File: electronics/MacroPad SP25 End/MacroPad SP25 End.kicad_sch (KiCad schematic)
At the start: 14 parts, among them J1 Conn_01x07_Pin, J2 Conn_01x07_Pin, J3 Conn_01x07_Pin, J4 Conn_01x07_Pin, SW1 RotaryEncoder_Switch, SW2 RotaryEncoder_Switch

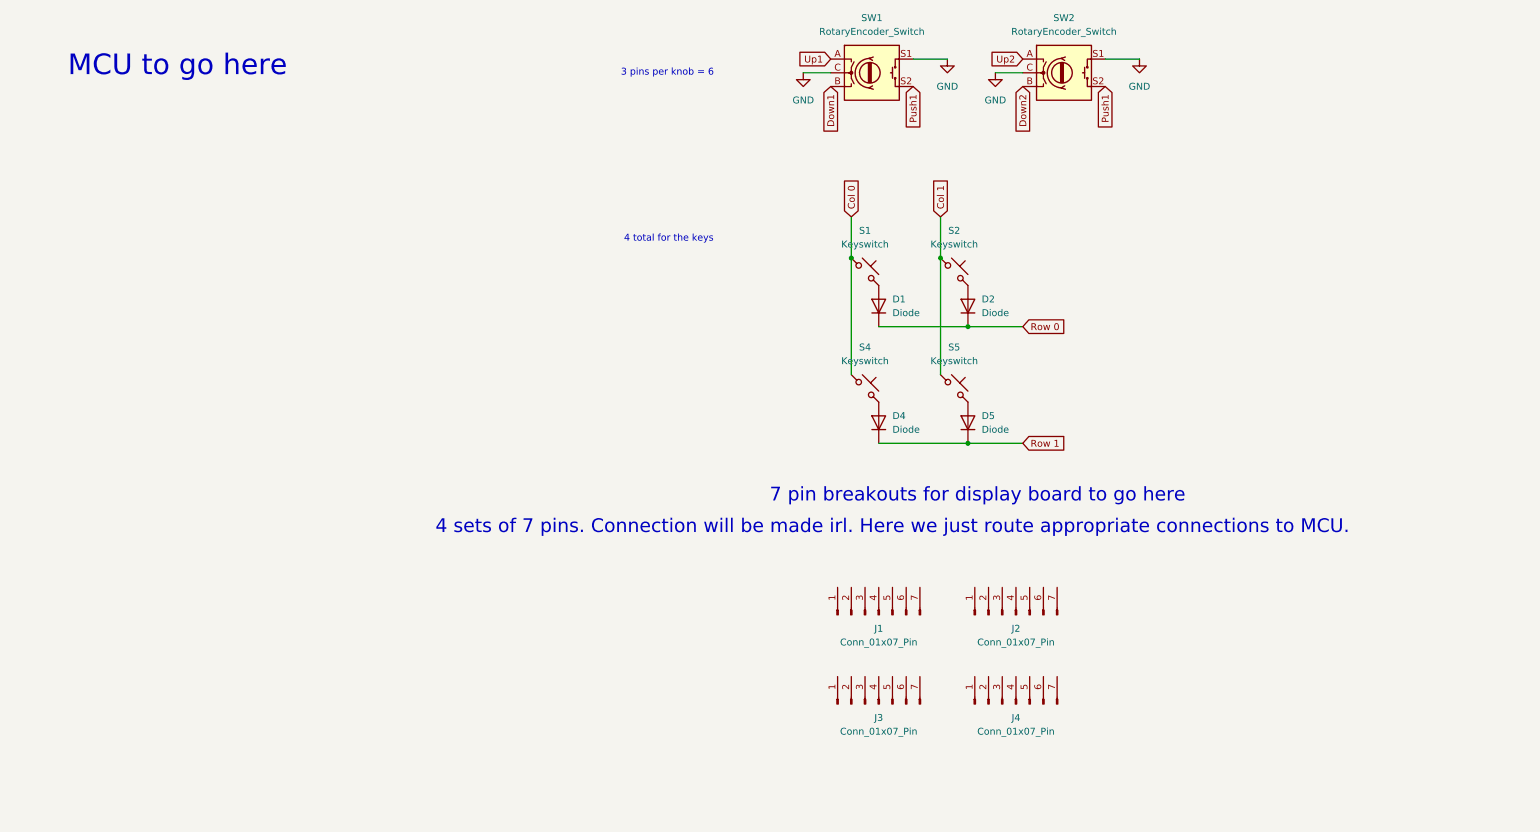
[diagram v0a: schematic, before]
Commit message: updated sp25 end -- wiring to esp and routing left
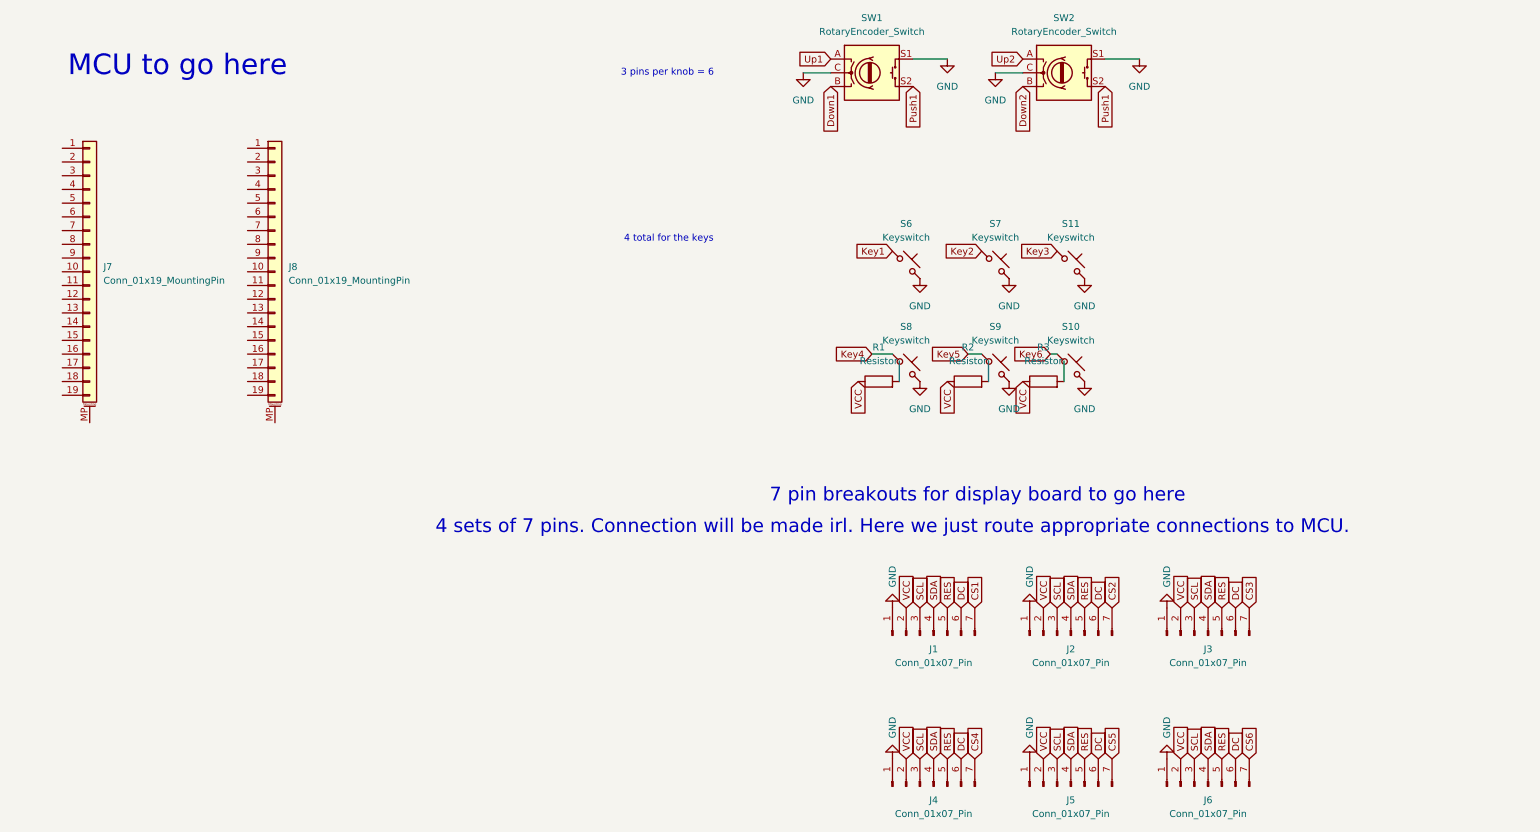
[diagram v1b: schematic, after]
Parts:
- removed D1, D2, D4, D5: Diode, ScottoKeebs_Components:Diode_DO-35, symbol ScottoKeebs:Placeholder_Diode
- removed S1, S2, S4, S5: Keyswitch, ScottoKeebs_MX:MX_PCB_1.00u, symbol ScottoKeebs:Placeholder_Keyswitch
- added J5, J6: Conn_01x07_Pin, Connector_PinHeader_2.54mm:PinHeader_1x07_P2.54mm_Vertical, symbol Connector:Conn_01x07_Pin
- added J7, J8: Conn_01x19_MountingPin, Connector_PinHeader_2.54mm:PinHeader_1x19_P2.54mm_Vertical, symbol Connector_Generic_MountingPin:Conn_01x19_MountingPin
- added R1, R2, R3: Resistor, ScottoKeebs_Components:Resistor_0402, symbol ScottoKeebs:Placeholder_Resistor
- added S10, S11, S6, S7, S8, S9: Keyswitch, ScottoKeebs_MX:MX_PCB_1.00u, symbol ScottoKeebs:Placeholder_Keyswitch
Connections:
- net GND: now also J1.1 (Pin_1), J2.1 (Pin_1), J3.1 (Pin_1), J4.1 (Pin_1), J5.1 (Pin_1), J6.1 (Pin_1), S10.2, S11.2, S6.2, S7.2, S8.2, S9.2
- net VCC: now reaches J3.2 (Pin_2)
- net VCC: now also J1.2 (Pin_2), J2.2 (Pin_2), J4.2 (Pin_2), J5.2 (Pin_2), J6.2 (Pin_2), R1.1, R2.1, R3.1
- net SCL: now reaches J3.3 (Pin_3)
- net SCL: now also J1.3 (Pin_3), J2.3 (Pin_3), J4.3 (Pin_3), J5.3 (Pin_3), J6.3 (Pin_3)
- net SDA: now reaches J3.4 (Pin_4)
- net SDA: now also J1.4 (Pin_4), J2.4 (Pin_4), J4.4 (Pin_4), J5.4 (Pin_4), J6.4 (Pin_4)
- net RES: now reaches J3.5 (Pin_5)
- net RES: now also J1.5 (Pin_5), J2.5 (Pin_5), J4.5 (Pin_5), J5.5 (Pin_5), J6.5 (Pin_5)
- net DC: now reaches J3.6 (Pin_6)
- net DC: now also J1.6 (Pin_6), J2.6 (Pin_6), J4.6 (Pin_6), J5.6 (Pin_6), J6.6 (Pin_6)
- net CS3: now reaches J3.7 (Pin_7)
- net CS1: now reaches J1.7 (Pin_7)
- net CS2: now reaches J2.7 (Pin_7)
- net CS4: now reaches J4.7 (Pin_7)
- new net CS5: J5.7 (Pin_7)
- new net CS6: J6.7 (Pin_7)
- new net Key1: S6.1
- new net Key2: S7.1
- new net Key3: S11.1
- new net Key4: S8.1
- new net Key5: S9.1
- new net Key6: S10.1
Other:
- moved on the sheet: J1, J2, J3, J4

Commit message: new sp25 ewnd
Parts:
- removed R1, R2, R3: Resistor, ScottoKeebs_Components:Resistor_0402, symbol ScottoKeebs:Placeholder_Resistor
- added R1, R2, R3, R4: 10k, Resistor_THT:R_Array_SIP4, symbol Device:R
- renumbered S6 to S1, S7 to S2, S11 to S3, S8 to S4, S9 to S5, S10 to S6
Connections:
- net CS1: now also J8.4 (Pin_4)
- net CS2: now also J8.10 (Pin_10)
- net CS3: now also J7.13 (Pin_13)
- net CS4: now also J7.12 (Pin_12)
- net CS5: now also J7.9 (Pin_9)
- net CS6: now also J7.8 (Pin_8)
- net DC: now also J8.5 (Pin_5)
- net Down1: now also J8.17 (Pin_17)
- net Down2: now also J8.8 (Pin_8)
- net GND: now also J8.19 (Pin_19)
- net Key1: now also J7.7 (Pin_7)
- net Key2: now also J8.12 (Pin_12)
- net Key3: now also J7.14 (Pin_14), R4.1
- net Key4: now also J7.17 (Pin_17), R1.1
- net Key5: now also J7.16 (Pin_16), R2.1
- net Key6: now also J7.15 (Pin_15), R3.1
- net Push1: now also J8.14 (Pin_14); no longer SW2.S2
- net RES: now also J8.7 (Pin_7)
- net SCL: now also J8.11 (Pin_11)
- net SDA: now also J8.18 (Pin_18)
- net Up1: now also J8.9 (Pin_9)
- net Up2: now also J7.11 (Pin_11)
- net VCC: now also J7.19 (Pin_19), R1.2, R2.2, R3.2, R4.2
- net Push2: now reaches J7.10 (Pin_10)
- net Push2: now also SW2.S2
